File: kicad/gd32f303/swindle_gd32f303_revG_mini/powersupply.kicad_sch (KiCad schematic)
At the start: 14 parts, among them J3 USB, U5 LM1117-3.3

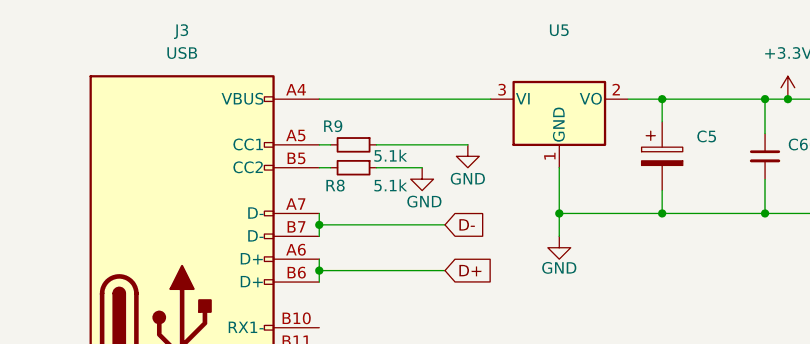
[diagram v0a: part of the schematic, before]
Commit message: add a WS2812b to the mini version, mini version for CH32,GD32 and RP2xxx
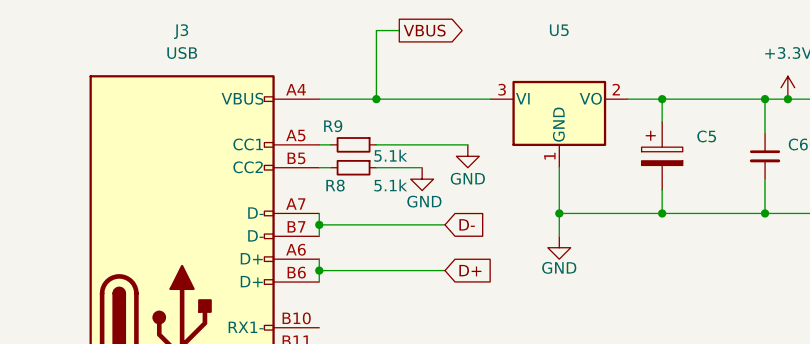
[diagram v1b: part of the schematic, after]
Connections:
- net VBUS: now reaches J3.A4 (VBUS), J3.A9 (VBUS), J3.B4 (VBUS), J3.B9 (VBUS), U5.3 (VI)
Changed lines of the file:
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@@
+	)
+	(junction
+		(at 102.87 48.26)
+		(diameter 0)
+		(color 0 0 0 0)
 	)
 	(junction
@@
 	(wire
 		(pts
+			(xy 102.87 48.26) (xy 115.57 48.26)
+		)
+		(stroke
+			(width 0)
+			(type default)
+		)
+	)
+	(wire
+		(pts
 			(xy 96.52 67.31) (xy 110.49 67.31)
 		)
@@
 	(wire
 		(pts
+			(xy 102.87 48.26) (xy 102.87 40.64)
+		)
+		(stroke
+			(width 0)
+			(type default)
+		)
+	)
+	(wire
+		(pts
 			(xy 30.48 153.67) (xy 30.48 154.94)
 		)
@@
 	(wire
 		(pts
+			(xy 102.87 40.64) (xy 105.41 40.64)
+		)
+		(stroke
+			(width 0)
+			(type default)
+		)
+	)
+	(wire
+		(pts
 			(xy 34.29 148.59) (xy 40.64 148.59)
 		)
@@
 	(wire
 		(pts
-			(xy 96.52 48.26) (xy 115.57 48.26)
+			(xy 96.52 48.26) (xy 102.87 48.26)
 		)
 		(stroke
@@
 			(effects
 				(font
+					(size 1.27 1.27)
+				)
+				(justify left)
+				(hide yes)
+			)
+		)
+	)
+	(global_label "VBUS"
+		(shape output)
+		(at 105.41 40.64 0)
+		(fields_autoplaced yes)
+		(effects
+			(font
+				(size 1.27 1.27)
+			)
+			(justify left)
+		)
+		(property "Intersheetrefs" "${INTERSHEET_REFS}"
+			(at 113.2938 40.64 0)
+			(effects
+				(font

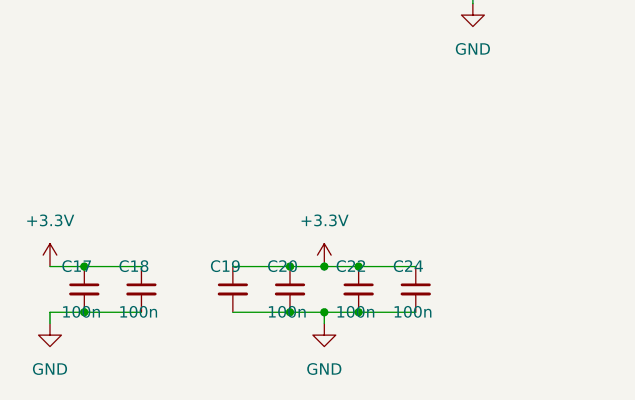
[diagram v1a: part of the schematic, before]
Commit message: kicad, gd32 mini: add back the boot0 pulldown (duh)
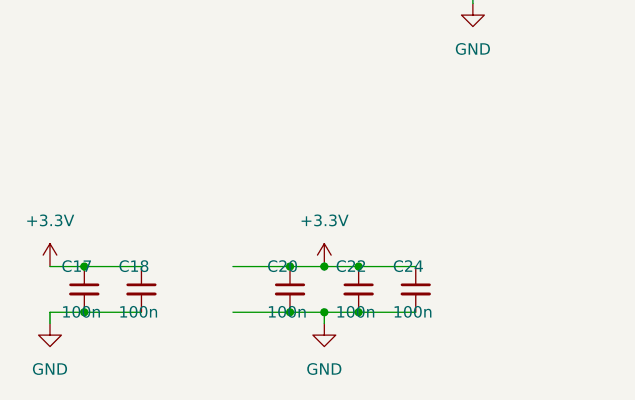
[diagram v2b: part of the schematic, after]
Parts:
- removed C19: 100n, Resistor_SMD:R_0603_1608Metric, symbol Device:C_Small
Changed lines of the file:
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@@
-	(symbol
-		(lib_id "Device:C_Small")
-		(at 50.8 151.13 0)
-		(unit 1)
-		(exclude_from_sim no)
-		(in_bom yes)
-		(on_board yes)
-		(dnp no)
-		(property "Reference" "C19"
-			(at 48.26 148.59 0)
-			(effects
-				(font
-					(size 1.27 1.27)
-				)
-				(justify left)
-			)
-		)
-		(property "Value" "100n"
-			(at 48.26 153.67 0)
-			(effects
-				(font
-					(size 1.27 1.27)
-				)
-				(justify left)
-				(hide yes)
-			)
-		)
-		(property "Footprint" "Resistor_SMD:R_0603_1608Metric"
-			(at 50.8 151.13 0)
-			(effects
-				(font
-					(size 1.27 1.27)
-				)
-				(hide yes)
-			)
-		)
-		(property "Datasheet" "~"
-			(at 50.8 151.13 0)
-			(effects
-				(font
-					(size 1.27 1.27)
-				)
-				(hide yes)
-			)
-		)
-		(property "Description" ""
-			(at 50.8 151.13 0)
-			(effects
-				(font
-					(size 1.27 1.27)
-				)
-				(hide yes)
-			)
-		)
-		(pin "1"
-		)
-		(pin "2"
-		)
-		(instances
-			(project "gd32f303_revG_mini"
-				(path "/fbe443d6-6d74-4abc-9dee-16e0160553bc/3e3374ff-17d6-414d-9a63-96aa322d3dc0"
-					(reference "C19")
-					(unit 1)
-				)
-			)
-		)
-	)
 	(symbol
 		(lib_id "Device:C_Small")
